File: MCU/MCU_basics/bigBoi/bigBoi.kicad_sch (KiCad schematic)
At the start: 39 parts, among them J4 Conn_01x05, J5 Conn_01x04, J6 Conn_01x06, J7 USB_B_Micro, SW1 Boot Switch, U1 STM32F469NIHx, Y1 8MHz

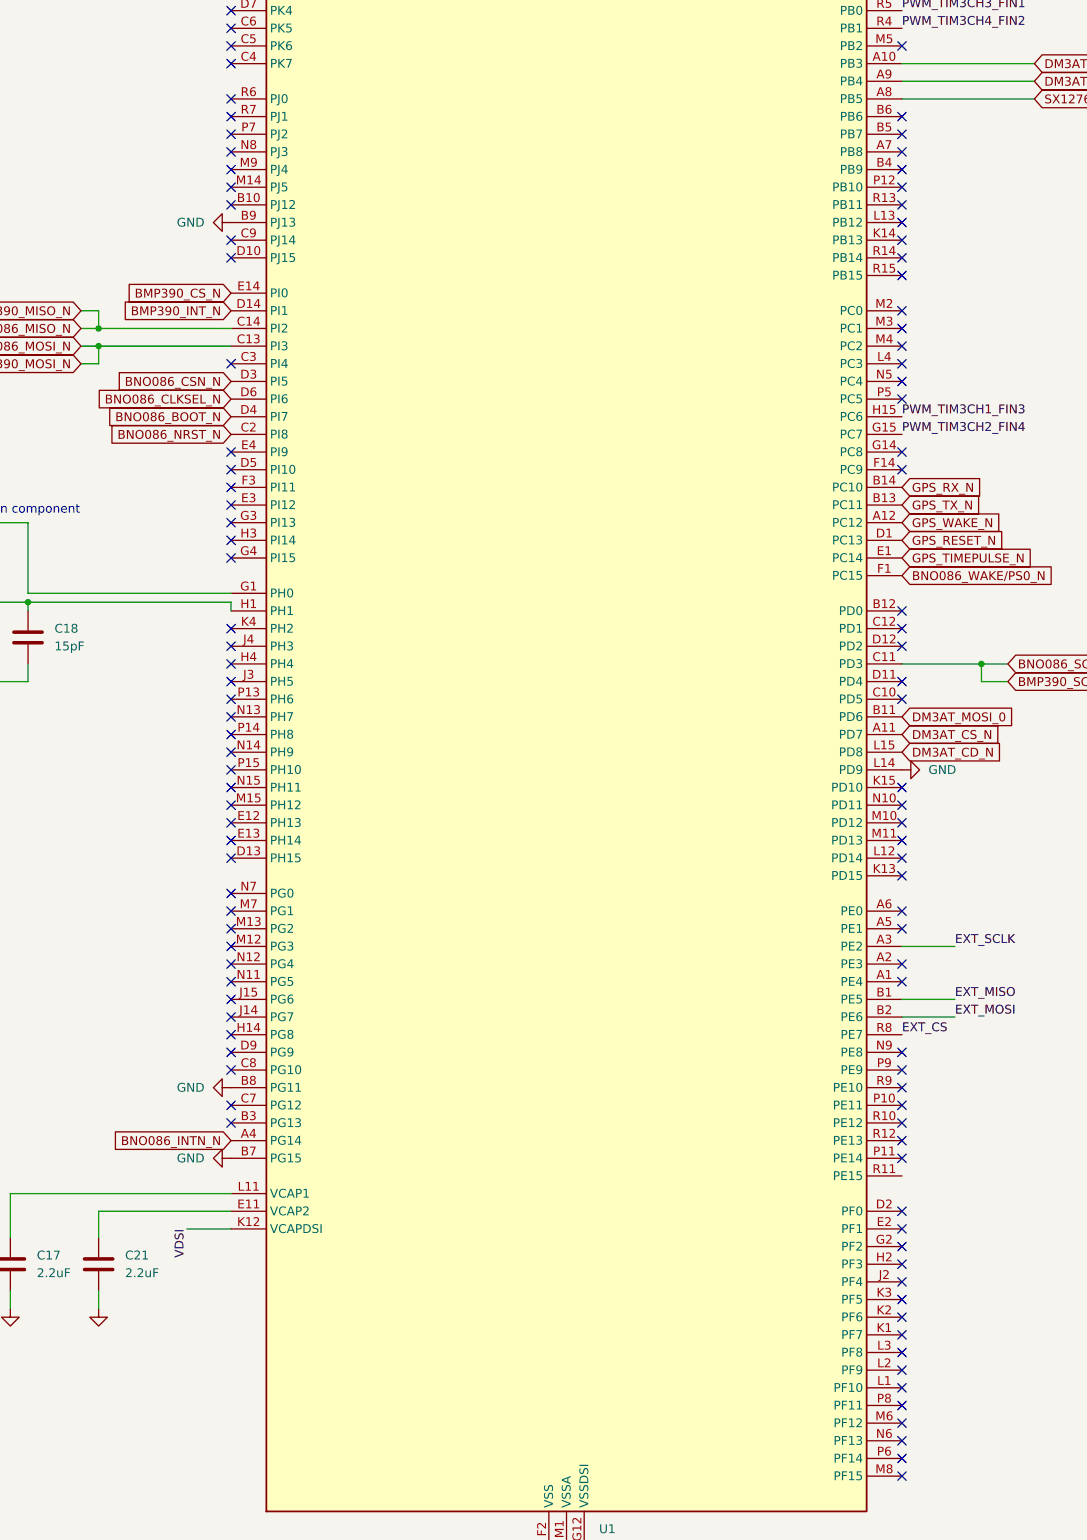
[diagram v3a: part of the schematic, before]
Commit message: MCU pwr+esc
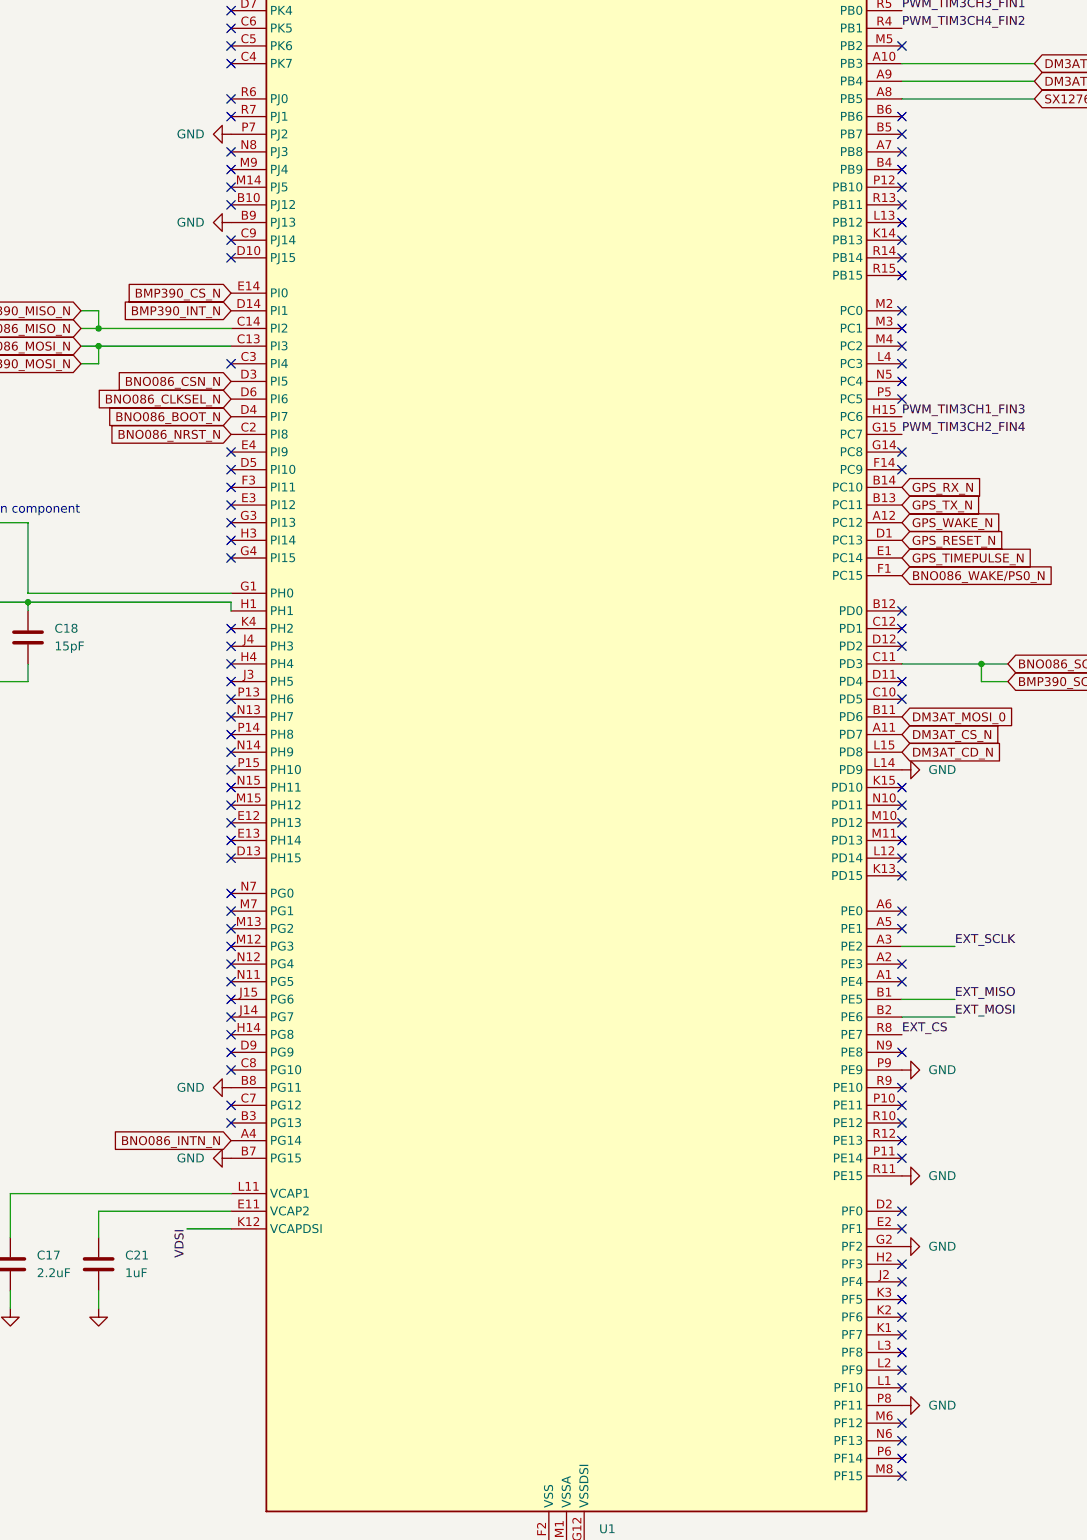
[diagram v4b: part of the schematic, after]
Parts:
- C21: value 2.2uF -> 1uF; footprint Capacitor_SMD:C_0603_1608Metric -> Capacitor_SMD:C_0402_1005Metric
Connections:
- net GND: now also U1.G2 (PF2), U1.P7 (PJ2), U1.P8 (PF11), U1.P9 (PE9), U1.R11 (PE15)
- no-connect marks 120 -> 116

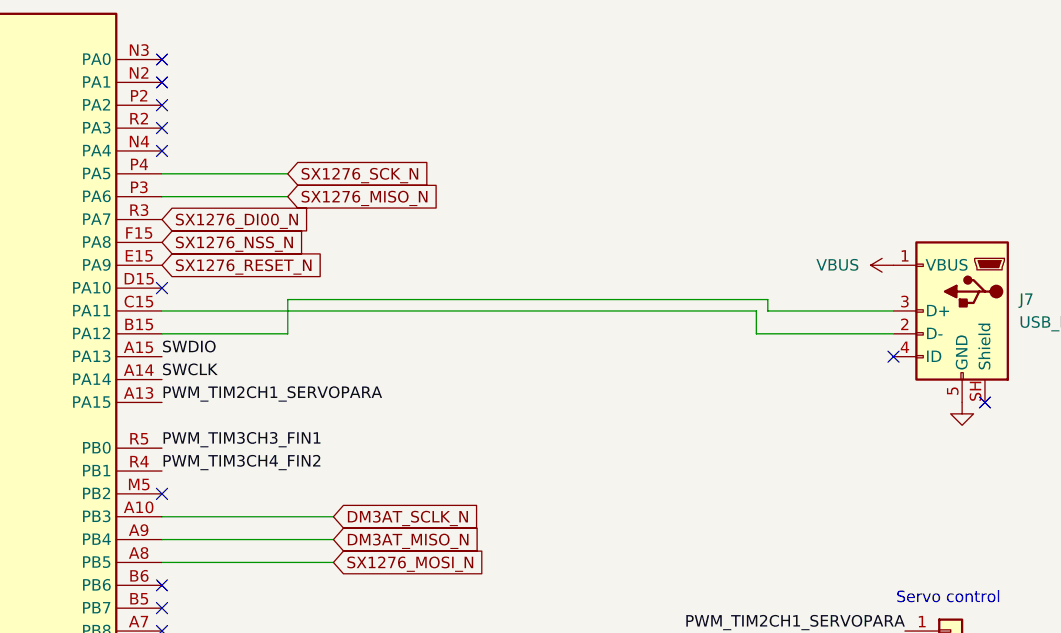
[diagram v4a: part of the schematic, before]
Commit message: Store deler av VBUS og USB
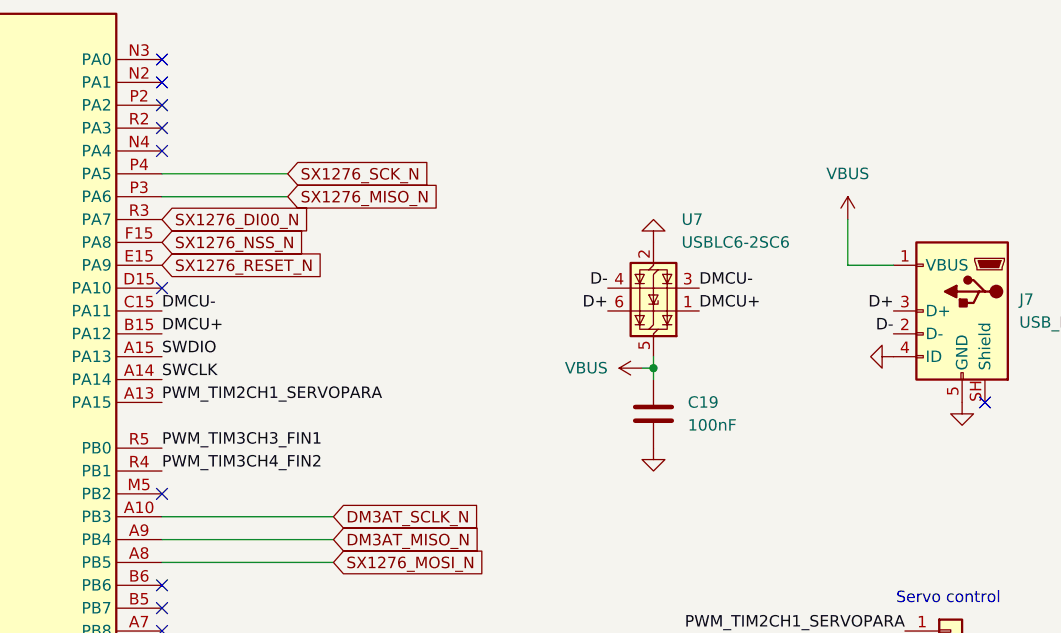
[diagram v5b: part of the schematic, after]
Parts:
- added C19: 100nF, Capacitor_SMD:C_0402_1005Metric, symbol Device:C
- added U7: USBLC6-2SC6, Package_TO_SOT_SMD:SOT-23-6, symbol Power_Protection:USBLC6-2SC6
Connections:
- net GND: now also J7.4 (ID), C19.2, U7.2 (GND)
- net VBUS: now also C19.1, U7.5 (VBUS)
- net D-: now reaches J7.2 (D-)
- net D-: now also U7.4 (I/O2); no longer U1.C15 (PA11)
- net D+: now reaches J7.3 (D+)
- net D+: now also U7.6 (I/O1); no longer U1.B15 (PA12)
- new net DMCU+: U1.B15 (PA12), U7.1 (I/O1)
- new net DMCU-: U1.C15 (PA11), U7.3 (I/O2)
- no-connect marks 116 -> 115

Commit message: SX1276 layout
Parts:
- Y1: footprint Crystal:Crystal_SMD_3225-4Pin_3.2x2.5mm_HandSoldering -> Crystal:Crystal_SMD_3225-4Pin_3.2x2.5mm
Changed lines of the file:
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@@
 			)
 		)
-		(property "Footprint" "Crystal:Crystal_SMD_3225-4Pin_3.2x2.5mm_HandSoldering"
+		(property "Footprint" "Crystal:Crystal_SMD_3225-4Pin_3.2x2.5mm"
 			(at 173.99 201.93 0)
 			(hide yes)

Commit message: routing complete
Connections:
- net GND: now also U1.C12 (PD1)
- no-connect marks 115 -> 114
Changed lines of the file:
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@@
 	)
 	(no_connect
-		(at 309.88 205.74)
-	)
-	(no_connect
 		(at 309.88 76.2)
 	)
@@
 					(unit 1)
 				)
+			)
+		)
+	)
+	(symbol
+		(lib_id "power:GND")
+		(at 309.88 205.74 90)
+		(unit 1)
+		(body_style 1)
+		(exclude_from_sim no)
+		(in_bom yes)
+		(on_board yes)
+		(in_pos_files yes)
+		(dnp no)
+		(fields_autoplaced yes)
+		(property "Reference" "#PWR092"
+			(at 316.23 205.74 0)
+			(hide yes)
+			(show_name no)
+			(do_not_autoplace no)
+			(effects
+				(font
+					(size 1.27 1.27)
+				)
+			)
+		)
+		(property "Value" "GND"
+			(at 313.69 205.7399 90)
+			(show_name no)
+			(do_not_autoplace no)
+			(effects
+				(font
+					(size 1.27 1.27)
+				)
+				(justify right)
+			)
+		)
+		(property "Footprint" ""
+			(at 309.88 205.74 0)
+			(hide yes)
+			(show_name no)
+			(do_not_autoplace no)
+			(effects
+				(font
+					(size 1.27 1.27)
+				)
+			)
+		)
+		(property "Datasheet" ""
+			(at 309.88 205.74 0)
+			(hide yes)
+			(show_name no)
+			(do_not_autoplace no)
+			(effects
+				(font
+					(size 1.27 1.27)
+				)
+			)
+		)
+		(property "Description" "Power symbol creates a global label with name \"GND\" , ground"
+			(at 309.88 205.74 0)
+			(hide yes)
+			(show_name no)
+			(do_not_autoplace no)
+			(effects
+				(font
+					(size 1.27 1.27)
+				)
+			)
+		)
+		(pin "1"
+		)
+		(instances
+			(project "bigBoi"
+				(path "/0a118c22-2522-42a6-b7a6-70c79326ece4"
+					(reference "#PWR092")
+					(unit 1)
+				)
